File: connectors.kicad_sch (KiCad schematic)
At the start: 6 parts, among them J1 Conn_01x02, J2 Conn_01x02, J3 Conn_01x04, J4 Conn_01x04, J5 USB_C_Receptacle_USB2.0

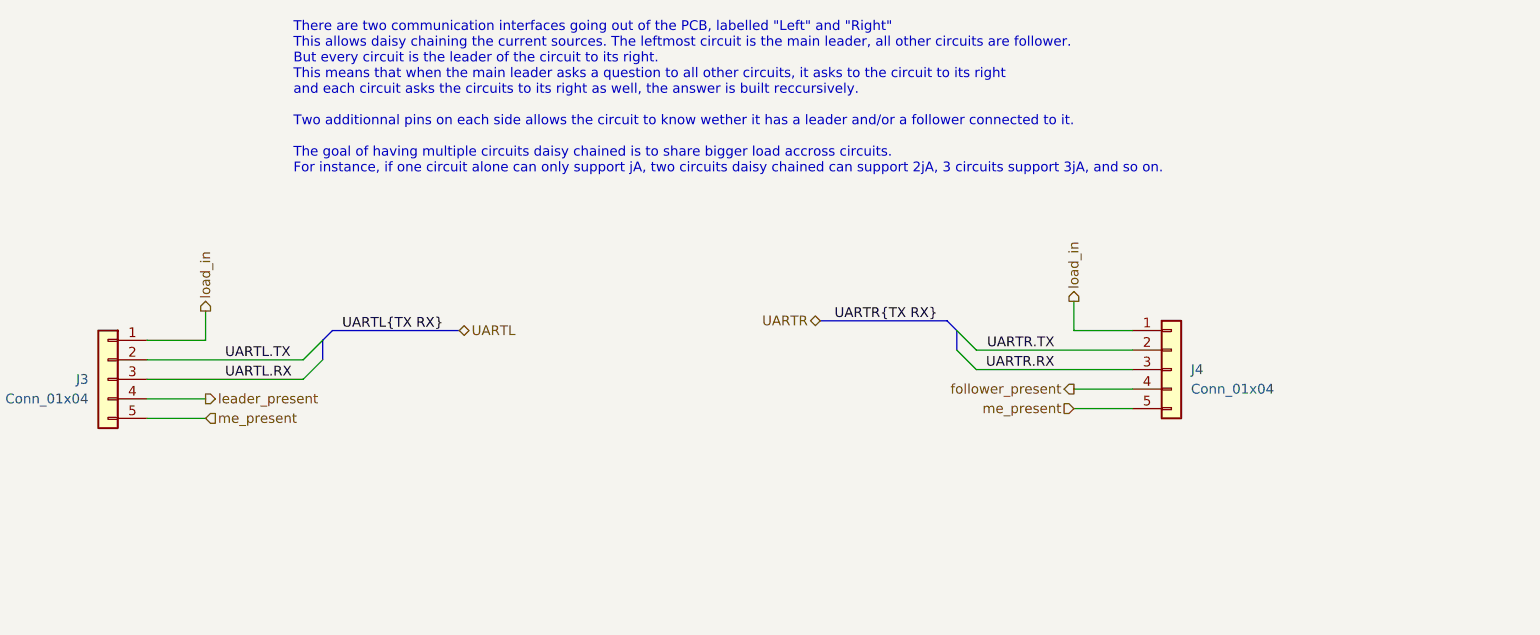
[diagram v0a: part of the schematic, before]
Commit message: Replace UART{R,L} with I2C
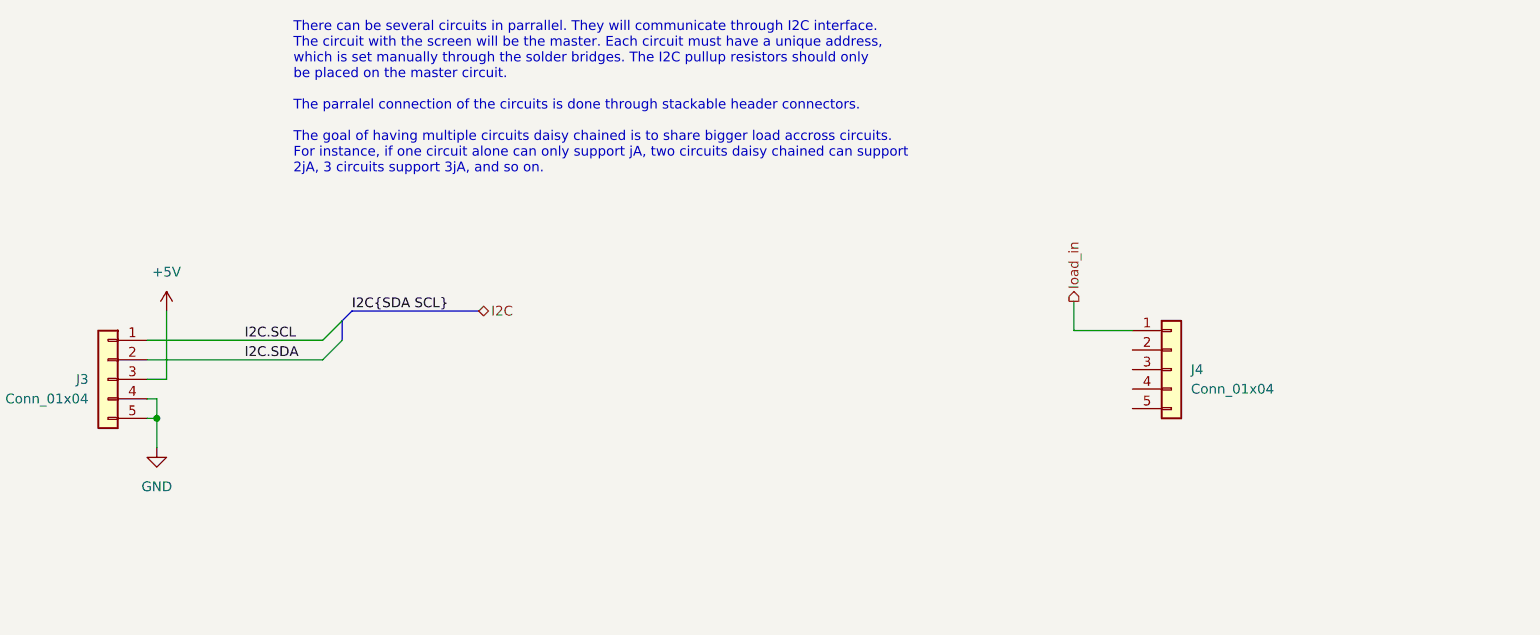
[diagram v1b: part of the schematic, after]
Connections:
- net leader_present is gone; now on net GND: J3.4 (Pin_4)
- net GND: now also J3.5 (Pin_5)
- net load_in: no longer J3.1 (Pin_1)
- net UARTL.RX renamed +5V
- net UARTL.TX renamed I2C.SDA
- net UARTR.RX: no longer names the net of J4.3 (Pin_3)
- net UARTR.TX: no longer names the net of J4.2 (Pin_2)
- net follower_present: no longer names the net of J4.4 (Pin_4)
- net me_present: no longer names the net of J4.5 (Pin_5)
- net me_present: no longer J3.5 (Pin_5)
- new net I2C.SCL: J3.1 (Pin_1)
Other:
- note added: "There can be several circuits in parrallel. They will communicate through I2C interface. The circuit with the screen will be the master. Each circuit must have a unique address, which is set manually through the solder bridges. The I2C pullup resistors should only be placed on the master circuit. The parralel connection of the circuits is done through stackable header connectors. The goal of havi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"
- note removed: "There are two communication interfaces going out of the PCB, labelled "Left" and "Right" This allows daisy chaining the current sources. The leftmost circuit is the main leader, all other circuits are follower. But every circuit is the leader of the circuit to its right. This means that when the main leader asks a question to all other circuits, it asks to the circuit to its right and each circui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"
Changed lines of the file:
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@@
 (kicad_sch (version 20211123) (generator eeschema)
   (paper "A4")
-  (bus_entry (at 154.94 58.42) (size -2.54 2.54)
-    (stroke (width 0) (type default) (color 0 0 0 0))
-  )
-  (bus_entry (at 154.94 60.96) (size -2.54 2.54)
-    (stroke (width 0) (type default) (color 0 0 0 0))
-  )
-  (bus_entry (at 237.49 57.15) (size 2.54 2.54)
-    (stroke (width 0) (type default) (color 0 0 0 0))
-  )
-  (bus_entry (at 237.49 59.69) (size 2.54 2.54)
+  (junction (at 133.35 68.58) (diameter 0) (color 0 0 0 0)
+  )
+  (bus_entry (at 157.48 55.88) (size -2.54 2.54)
+    (stroke (width 0) (type default) (color 0 0 0 0))
+  )
+  (bus_entry (at 157.48 58.42) (size -2.54 2.54)
     (stroke (width 0) (type default) (color 0 0 0 0))
   )
@@
     (stroke (width 0) (type default) (color 0 0 0 0))
   )
-  (bus (pts (xy 237.49 57.15) (xy 237.49 59.69))
-    (stroke (width 0) (type default) (color 0 0 0 0))
-  )
-  (bus (pts (xy 154.94 58.42) (xy 154.94 60.96))
-    (stroke (width 0) (type default) (color 0 0 0 0))
-  )
-  (wire (pts (xy 132.08 63.5) (xy 152.4 63.5))
+  (bus (pts (xy 158.75 54.61) (xy 157.48 55.88))
+    (stroke (width 0) (type default) (color 0 0 0 0))
+  )
+  (wire (pts (xy 132.08 68.58) (xy 133.35 68.58))
+    (stroke (width 0) (type default) (color 0 0 0 0))
+  )
+  (wire (pts (xy 132.08 58.42) (xy 154.94 58.42))
+    (stroke (width 0) (type default) (color 0 0 0 0))
+  )
+  (wire (pts (xy 132.08 63.5) (xy 134.62 63.5))
     (stroke (width 0) (type default) (color 0 0 0 0))
   )
@@
     (stroke (width 0) (type default) (color 0 0 0 0))
   )
-  (wire (pts (xy 139.7 54.61) (xy 139.7 58.42))
-    (stroke (width 0) (type default) (color 0 0 0 0))
-  )
-  (wire (pts (xy 139.7 58.42) (xy 132.08 58.42))
-    (stroke (width 0) (type default) (color 0 0 0 0))
-  )
-  (bus (pts (xy 172.72 57.15) (xy 156.21 57.15))
+  (wire (pts (xy 133.35 72.39) (xy 133.35 68.58))
+    (stroke (width 0) (type default) (color 0 0 0 0))
+  )
+  (wire (pts (xy 132.08 60.96) (xy 154.94 60.96))
+    (stroke (width 0) (type default) (color 0 0 0 0))
+  )
+  (wire (pts (xy 133.35 68.58) (xy 133.35 66.04))
     (stroke (width 0) (type default) (color 0 0 0 0))
   )
@@
     (stroke (width 0) (type default) (color 0 0 0 0))
   )
-  (wire (pts (xy 240.03 59.69) (xy 260.35 59.69))
-    (stroke (width 0) (type default) (color 0 0 0 0))
-  )
-  (wire (pts (xy 132.08 68.58) (xy 139.7 68.58))
+  (wire (pts (xy 134.62 54.61) (xy 134.62 63.5))
+    (stroke (width 0) (type default) (color 0 0 0 0))
+  )
+  (wire (pts (xy 133.35 66.04) (xy 132.08 66.04))
     (stroke (width 0) (type default) (color 0 0 0 0))
   )
@@
     (stroke (width 0) (type default) (color 0 0 0 0))
   )
-  (wire (pts (xy 252.73 64.77) (xy 260.35 64.77))
-    (stroke (width 0) (type default) (color 0 0 0 0))
-  )
-  (wire (pts (xy 252.73 67.31) (xy 260.35 67.31))
-    (stroke (width 0) (type default) (color 0 0 0 0))
-  )
-  (bus (pts (xy 219.71 55.88) (xy 236.22 55.88))
-    (stroke (width 0) (type default) (color 0 0 0 0))
-  )
-  (wire (pts (xy 132.08 66.04) (xy 139.7 66.04))
-    (stroke (width 0) (type default) (color 0 0 0 0))
-  )
-  (wire (pts (xy 132.08 60.96) (xy 152.4 60.96))
-    (stroke (width 0) (type default) (color 0 0 0 0))
-  )
-  (bus (pts (xy 156.21 57.15) (xy 154.94 58.42))
-    (stroke (width 0) (type default) (color 0 0 0 0))
-  )
-  (wire (pts (xy 240.03 62.23) (xy 260.35 62.23))
-    (stroke (width 0) (type default) (color 0 0 0 0))
-  )
-  (bus (pts (xy 236.22 55.88) (xy 237.49 57.15))
+  (bus (pts (xy 175.26 54.61) (xy 158.75 54.61))
+    (stroke (width 0) (type default) (color 0 0 0 0))
+  )
+  (bus (pts (xy 157.48 55.88) (xy 157.48 58.42))
     (stroke (width 0) (type default) (color 0 0 0 0))
   )
@@
     (effects (font (size 1.27 1.27)) (justify left bottom))
   )
-  (text "There are two communication interfaces going out of the PCB, labelled \"Left\" and \"Right\"\nThis allows daisy chaining the current sources. The leftmost circuit is the main leader, all other circuits are follower. \nBut every circuit is the leader of the circuit to its right.\nThis means that when the main leader asks a question to all other circuits, it asks to the circuit to its right\nand each circuit asks the circuits to its right as well, the answer is built reccursively.\n\nTwo additionnal pins on each side allows the circuit to know wether it has a leader and/or a follower connected to it.\n\nThe goal of having multiple circuits daisy chained is to share bigger load accross circuits.\nFor instance, if one circuit alone can only support jA, two circuits daisy chained can support 2jA, 3 circuits support 3jA, and so on."
+  (text "There can be several circuits in parrallel. They will communicate through I2C interface.\nThe circuit with the screen will be the master. Each circuit must have a unique address, \nwhich is set manually through the solder bridges. The I2C pullup resistors should only \nbe placed on the master circuit.\n\nThe parralel connection of the circuits is done through stackable header connectors.\n\nThe goal of having multiple circuits daisy chained is to share bigger load accross circuits.\nFor instance, if one circuit alone can only support jA, two circuits daisy chained can support \n2jA, 3 circuits support 3jA, and so on."
     (at 151.13 36.83 0)
     (effects (font (size 1.27 1.27)) (justify left bottom))
@@
     (effects (font (size 1.27 1.27)) (justify left bottom))
   )
-  (label "UARTR.TX" (at 250.19 59.69 180)
-    (effects (font (size 1.27 1.27)) (justify right bottom))
-  )
-  (label "UARTR.RX" (at 250.19 62.23 180)
-    (effects (font (size 1.27 1.27)) (justify right bottom))
-  )
-  (label "UARTR{TX RX}" (at 234.95 55.88 180)
-    (effects (font (size 1.27 1.27)) (justify right bottom))
-  )
-  (label "UARTL.TX" (at 142.24 60.96 0)
-    (effects (font (size 1.27 1.27)) (justify left bottom))
-  )
-  (label "UARTL{TX RX}" (at 157.48 57.15 0)
-    (effects (font (size 1.27 1.27)) (justify left bottom))
-  )
-  (label "UARTL.RX" (at 142.24 63.5 0)
-    (effects (font (size 1.27 1.27)) (justify left bottom))
-  )
-  (hierarchical_label "me_present" (shape input) (at 252.73 67.31 180)
-    (effects (font (size 1.27 1.27)) (justify right))
+  (label "I2C.SDA" (at 144.78 60.96 0)
+    (effects (font (size 1.27 1.27)) (justify left bottom))
+  )
+  (label "I2C.SCL" (at 144.78 58.42 0)
+    (effects (font (size 1.27 1.27)) (justify left bottom))
+  )
+  (label "I2C{SDA SCL}" (at 158.75 54.61 0)
+    (effects (font (size 1.27 1.27)) (justify left bottom))
   )
   (hierarchical_label "load_in" (shape output) (at 252.73 53.34 90)
     (effects (font (size 1.27 1.27)) (justify left))
   )
-  (hierarchical_label "UARTR" (shape bidirectional) (at 219.71 55.88 180)
-    (effects (font (size 1.27 1.27)) (justify right))
-  )
-  (hierarchical_label "UARTL" (shape bidirectional) (at 172.72 57.15 0)
-    (effects (font (size 1.27 1.27)) (justify left))
-  )
-  (hierarchical_label "me_present" (shape input) (at 139.7 68.58 0)
-    (effects (font (size 1.27 1.27)) (justify left))
-  )
   (hierarchical_label "load_in" (shape output) (at 46.99 48.26 0)
     (effects (font (size 1.27 1.27)) (justify left))
   )
-  (hierarchical_label "leader_present" (shape output) (at 139.7 66.04 0)
-    (effects (font (size 1.27 1.27)) (justify left))
-  )
-  (hierarchical_label "follower_present" (shape output) (at 252.73 64.77 180)
-    (effects (font (size 1.27 1.27)) (justify right))
-  )
-  (hierarchical_label "load_in" (shape output) (at 139.7 54.61 90)
+  (hierarchical_label "I2C" (shape bidirectional) (at 175.26 54.61 0)
     (effects (font (size 1.27 1.27)) (justify left))
   )
@@
     (pin "1")
     (pin "2")
+  )
+  (symbol (lib_id "power:+5V") (at 134.62 54.61 0) (unit 1)
+    (in_bom yes) (on_board yes) (fields_autoplaced)
+    (property "Reference" "#PWR?" (id 0) (at 134.62 58.42 0)
+      (effects (font (size 1.27 1.27)) hide)
+    )
+    (property "Value" "+5V" (id 1) (at 134.62 49.53 0))
+    (property "Footprint" "" (id 2) (at 134.62 54.61 0)
+      (effects (font (size 1.27 1.27)) hide)
+    )
+    (property "Datasheet" "" (id 3) (at 134.62 54.61 0)
+      (effects (font (size 1.27 1.27)) hide)
+    )
+    (pin "1")
   )
   (symbol (lib_id "Connector_Generic:Conn_01x02") (at 38.1 77.47 0) (mirror y) (unit 1)
@@
     (pin "5")
   )
+  (symbol (lib_id "power:GND") (at 133.35 72.39 0) (unit 1)
+    (in_bom yes) (on_board yes) (fields_autoplaced)
+    (property "Reference" "#PWR?" (id 0) (at 133.35 78.74 0)
+      (effects (font (size 1.27 1.27)) hide)
+    )
+    (property "Value" "GND" (id 1) (at 133.35 77.47 0))
+    (property "Footprint" "" (id 2) (at 133.35 72.39 0)
+      (effects (font (size 1.27 1.27)) hide)
+    )
+    (property "Datasheet" "" (id 3) (at 133.35 72.39 0)
+      (effects (font (size 1.27 1.27)) hide)
+    )
+    (pin "1")
+  )
 )

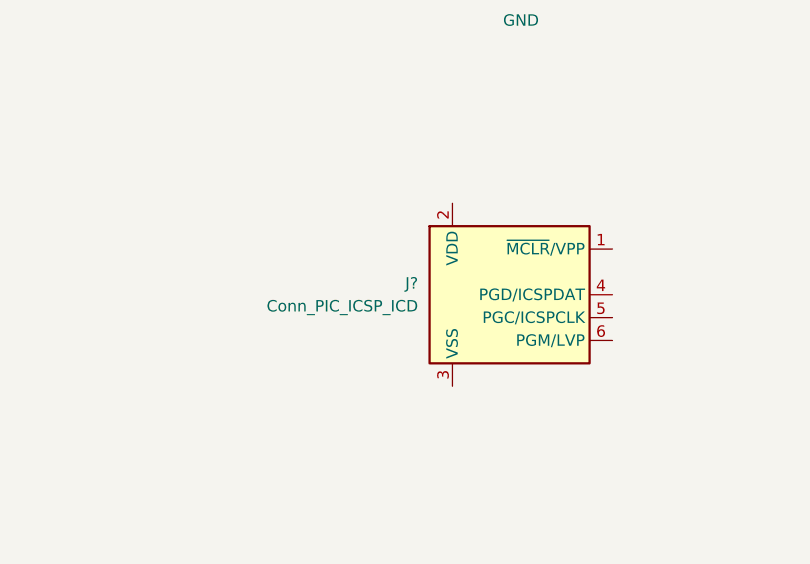
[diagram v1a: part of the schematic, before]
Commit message: Add voltage reference and voltage regulator
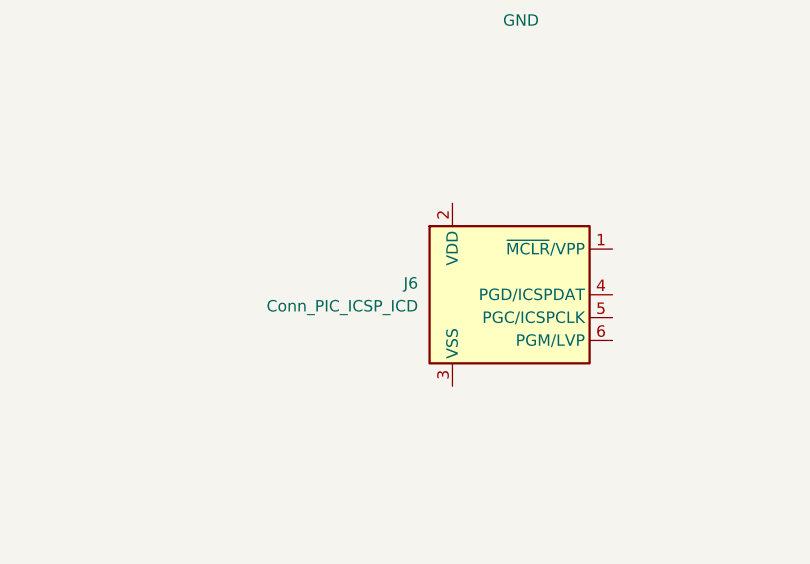
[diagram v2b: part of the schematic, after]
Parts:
- gave numbers to parts that had none: 1
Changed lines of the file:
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@@
   (symbol (lib_id "Connector:Conn_PIC_ICSP_ICD") (at 130.81 107.95 0) (unit 1)
     (in_bom yes) (on_board yes) (fields_autoplaced)
-    (property "Reference" "J?" (id 0) (at 121.92 106.6799 0)
+    (property "Reference" "J6" (id 0) (at 121.92 106.6799 0)
       (effects (font (size 1.27 1.27)) (justify right))
     )
@@
   (symbol (lib_id "power:+5V") (at 134.62 54.61 0) (unit 1)
     (in_bom yes) (on_board yes) (fields_autoplaced)
-    (property "Reference" "#PWR?" (id 0) (at 134.62 58.42 0)
+    (property "Reference" "#PWR0113" (id 0) (at 134.62 58.42 0)
       (effects (font (size 1.27 1.27)) hide)
     )
@@
   (symbol (lib_id "power:GND") (at 133.35 72.39 0) (unit 1)
     (in_bom yes) (on_board yes) (fields_autoplaced)
-    (property "Reference" "#PWR?" (id 0) (at 133.35 78.74 0)
+    (property "Reference" "#PWR0114" (id 0) (at 133.35 78.74 0)
       (effects (font (size 1.27 1.27)) hide)
     )
